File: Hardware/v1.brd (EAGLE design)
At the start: 77.5 x 32.6 mm, 54 parts, among them CN1 629105150521, CN2 TSW-120-08-L-S-RA, CN3 1734354-1, CN4 1-1734530-1, IC1 ADUM3160BRWZ, IC2 TUSB2046BIRHBT, IC3 IC_MAX3313, IC4 FT2232D, IC6 PCM2903C

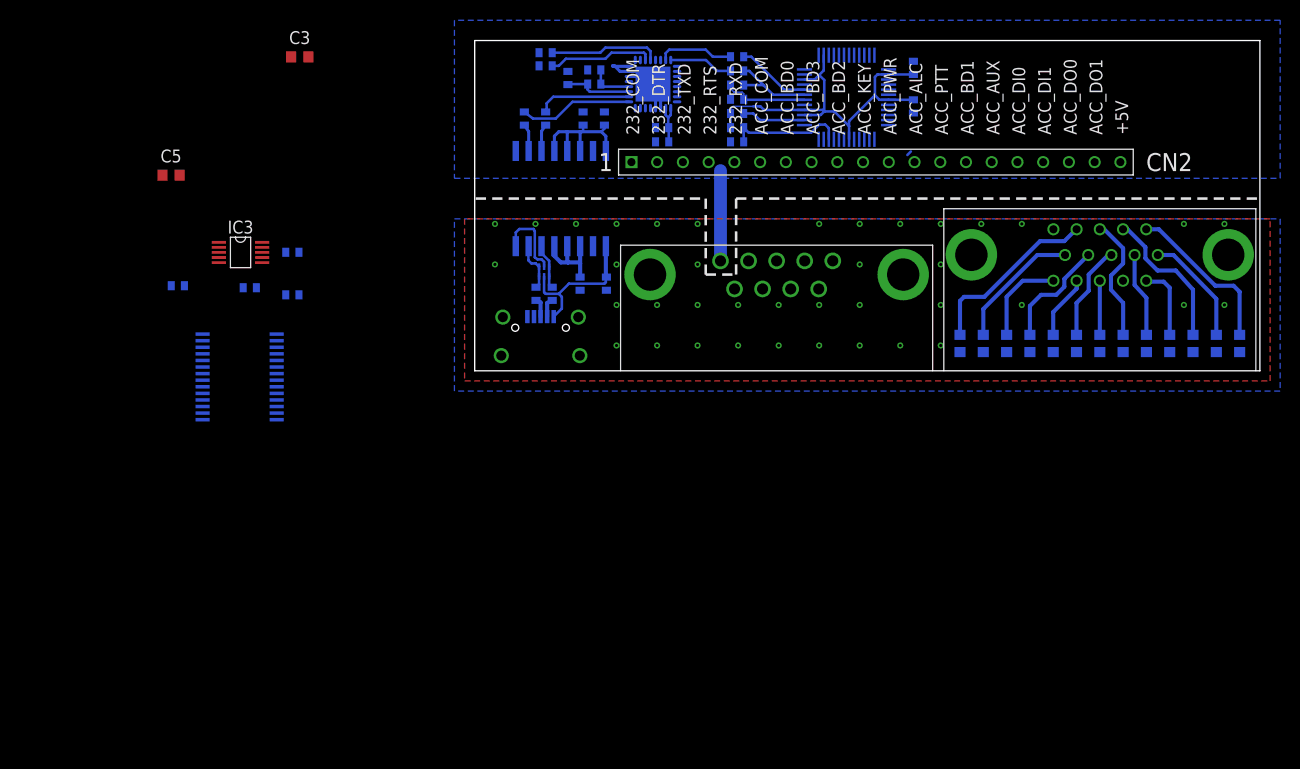
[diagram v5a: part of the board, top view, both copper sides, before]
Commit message: mirrored digital section of board to allow for easier routing to io
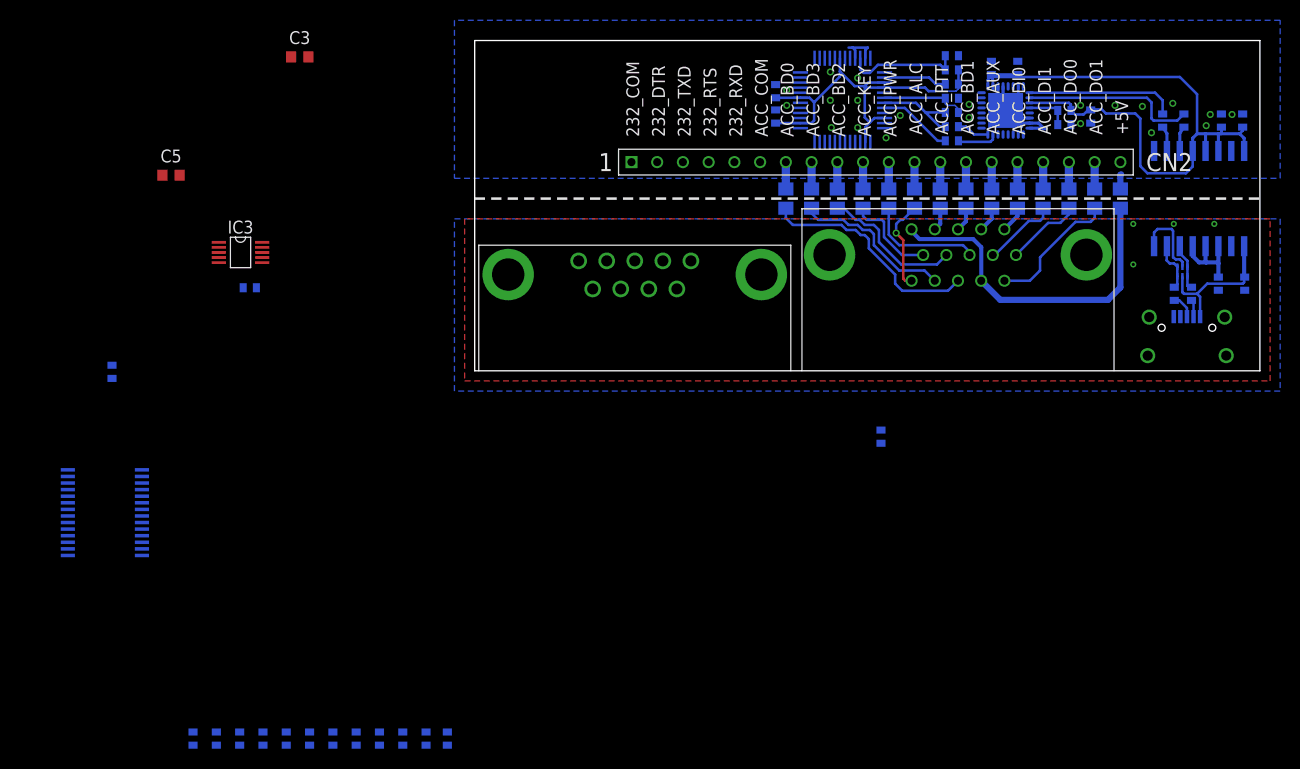
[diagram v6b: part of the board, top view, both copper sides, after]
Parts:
- removed R12, R13, R8, R9: 24, rcl:R0402
- added L1: 100uH, m0wut:R0805
- added R17, R18, R19, R20, R21, R22, R23, R24, R25, R26, R27, R28: 220, rcl:R0805
- added R29: 137k, rcl:R0805
- C12, C13, C14, C15, C16, C17, C18, C19, C20, C21, C22, C23, C24: device rcl:C0603 -> rcl:C0402
- moved C12 87.4 mm to (-2.70, -36.3)
- moved C13 87.2 mm to (-7.10, -36.3)
- moved C14 87.2 mm to (-14.0, -36.3)
- moved C16 87.2 mm to (-4.80, -36.3)
- moved C17 87.2 mm to (-11.7, -36.3)
- moved C18 87.2 mm to (-18.6, -36.3)
- moved C19 87.2 mm to (-23.2, -36.3)
- moved C20 87.2 mm to (-27.8, -36.3)
- moved C21 87.2 mm to (-9.40, -36.3)
- moved C22 87.2 mm to (-16.3, -36.3)
- moved C23 87.2 mm to (-20.9, -36.3)
- moved C24 87.2 mm to (-25.5, -36.3)
- moved CN1 63.8 mm to (70.3, 0.00)
- moved R2 63.1 mm to (70.8, 7.60)
- moved R4 63.0 mm to (67.9, 24.7)
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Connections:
- net N$4 renamed USB4_P
- net N$5 renamed USB4_N
- removed net DM1: R8.1
- removed net DM3: R13.2
- removed net DP1: R9.1
- removed net DP3: R12.2
- removed net N$18: C23.1, CN4.14
- removed net N$19: CN4.12
- removed net N$20: CN4.5
- removed net N$21: C24.1, CN4.15
- removed net N$22: C22.1, CN4.13
- removed net N$23: C21.1, CN4.11
- removed net N$24: C20.1, CN4.10
- removed net N$25: C19.1, CN4.9
- removed net N$26: C18.1, CN4.8
- removed net N$27: C17.1, CN4.7
- removed net N$28: C16.1, CN4.6
- removed net N$29: C15.1, CN4.4
- removed net N$30: C14.1, CN4.3
- removed net N$31: C13.1, CN4.2
- removed net N$32: C12.1, CN4.1
- new net 232_COM: CN2.P$1
- new net 232_DTR: CN2.P$2
- new net 232_RTS: CN2.P$4
- new net 232_RXD: CN2.P$5
- new net 232_TXD: CN2.P$3
- new net 5V_IN: CN2.P$20
- new net ACC_ALC: CN2.P$12, R29.1
- new net ACC_AUX: CN2.P$15, R18.1
- new net ACC_BND0: CN2.P$7, R27.1
- new net ACC_BND1: CN2.P$14, R19.1
- new net ACC_BND2: CN2.P$9, R24.1
- new net ACC_BND3: CN2.P$8, R28.1
- new net ACC_COM: CN2.P$6
- new net ACC_COMMON: CN4.12, CN4.5, L1.2
- new net ACC_DI0: CN2.P$16, R17.1
- new net ACC_DI1: CN2.P$17, R22.1
- new net ACC_DO0: CN2.P$18, R21.1
- new net ACC_DO1: CN2.P$19, R26.1
- new net ACC_KEY: CN2.P$10, R25.1
- new net ACC_PTT: CN2.P$13, R20.1
- new net ACC_PWR: CN2.P$11, R23.1
- new net ALC_X: C24.1, CN4.15, R29.2
- new net AUX_X: C13.1, CN4.2, R18.2
- new net BND0_X: C22.1, CN4.13, R27.2
- new net BND1_X: C14.1, CN4.3, R19.2
- new net BND2_X: C19.1, CN4.9, R24.2
- new net BND3_X: C23.1, CN4.14, R28.2
- new net DIG0_X: C12.1, CN4.1, R17.2
- new net DIG1_X: C17.1, CN4.7, R22.2
- new net DIGO1_X: C21.1, CN4.11, R26.2
- new net DIGO_X: C16.1, CN4.6, R21.2
- new net KEY_X: C20.1, CN4.10, R25.2
- new net PTT_X: C15.1, CN4.4, R20.2
- new net PWR_X: C18.1, CN4.8, R23.2
- net GND: now also L1.1
- net N$12: no longer R8.2
- net N$13: no longer R9.2
- net N$16: no longer R12.1
- net N$17: no longer R13.1
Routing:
- net +3V3: track 24.8 -> 68.5 mm
- net ACC_COMMON: track 0.00 -> 33.9 mm
- net BND0_X: track 0.00 -> 22.4 mm
- net N$29: track 17.8 -> 0.00 mm
- net BND3_X: track 0.00 -> 16.1 mm
- net N$32: track 16.0 -> 0.00 mm
- net N$31: track 14.5 -> 0.00 mm
- net BND2_X: track 0.00 -> 14.4 mm
- net DIGO1_X: track 0.00 -> 13.2 mm
- net N$24: track 12.8 -> 0.00 mm
- net N$30: track 12.6 -> 0.00 mm
- net PWR_X: track 0.00 -> 11.6 mm
- net N$28: track 11.1 -> 0.00 mm
- net N$25: track 11.1 -> 0.00 mm
- net N$13: track 10.9 -> 0.00 mm
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
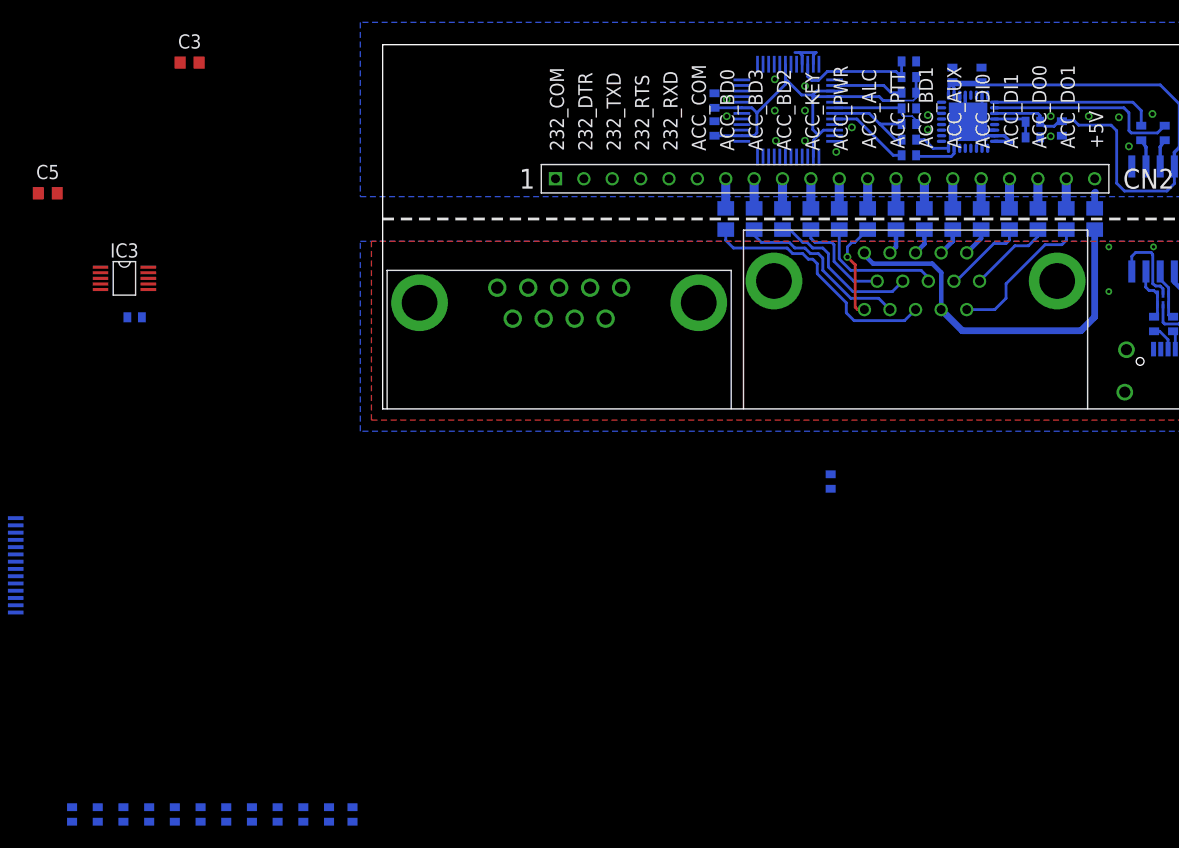
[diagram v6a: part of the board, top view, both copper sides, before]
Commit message: finally got the decoupling caps for the db15 to fit
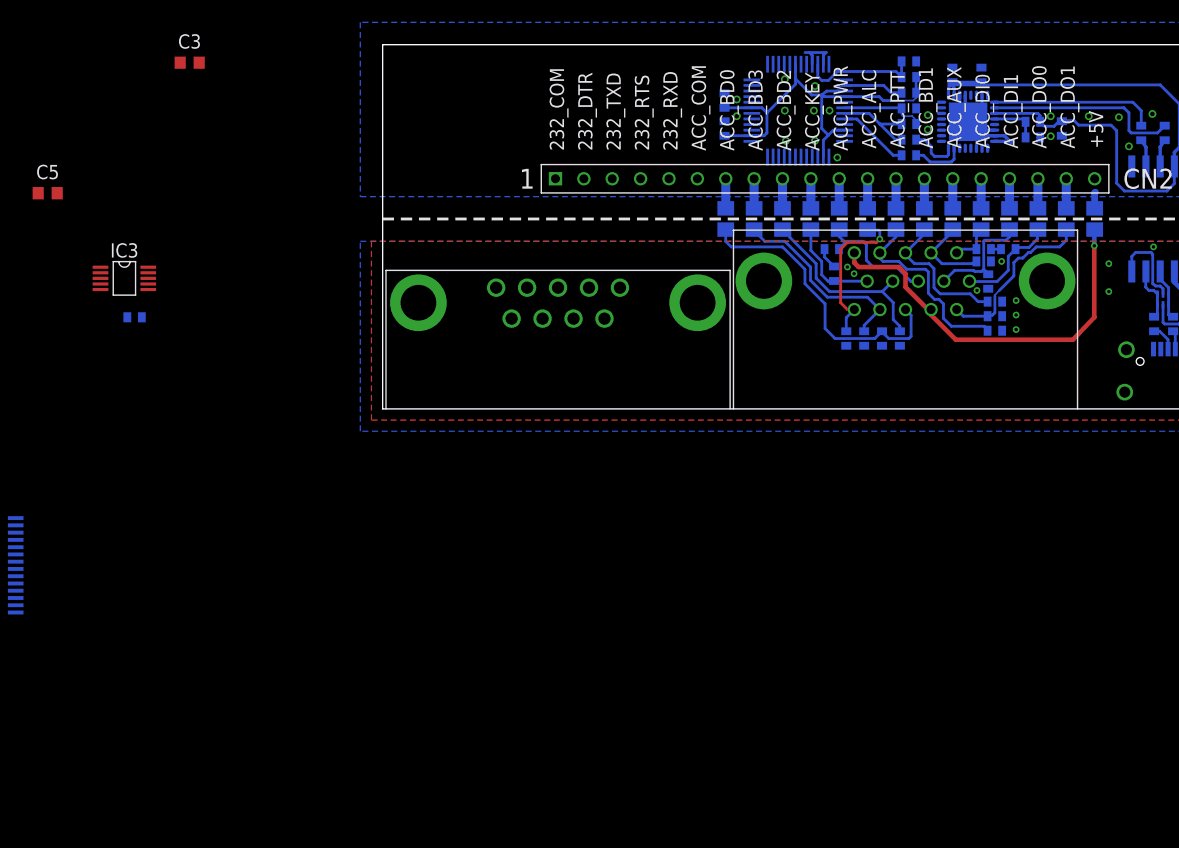
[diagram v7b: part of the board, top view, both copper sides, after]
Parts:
- moved C20 83.6 mm to (40.4, 12.1), turned to 90 degrees
- moved C14 82.7 mm to (54.8, 9.60), turned to 180 degrees
- moved C19 81.5 mm to (46.3, 6.30)
- moved C17 81.4 mm to (54.2, 11.4)
- moved C24 79.4 mm to (41.5, 6.30)
- moved C16 79.1 mm to (56.0, 14.3), turned to 0 degrees
- moved C13 78.5 mm to (53.8, 13.2), turned to 180 degrees
- moved C21 78.2 mm to (54.8, 8.30), turned to 180 degrees
- moved C18 77.6 mm to (40.2, 14.3), turned to 0 degrees
- moved C23 76.9 mm to (43.1, 6.30)
- moved C12 75.8 mm to (53.8, 14.3), turned to 180 degrees
- moved C22 74.4 mm to (44.7, 6.30)
- moved C15 20.0 mm to (54.8, 7.00), turned to 180 degrees
- moved CN4 0.90 mm to (46.8, 0.00)
- moved IC4 0.90 mm to (37.2, 26.7)
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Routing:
- net PTT_X: track 2.30 -> 17.4 mm
- net BND1_X: track 2.41 -> 13.0 mm
- net ALC_X: track 9.05 -> 14.2 mm
- net AUX_X: track 2.51 -> 7.43 mm
- net BND0_X: track 22.4 -> 26.5 mm
- net BND2_X: track 14.4 -> 18.4 mm
- net AGND: track 7.65 -> 10.7 mm, vias 4 -> 11
- net DIG1_X: track 7.44 -> 10.4 mm
- net DIGO_X: track 7.49 -> 9.93 mm
- net DIGO1_X: track 13.2 -> 15.5 mm
- net BND3_X: track 16.1 -> 17.5 mm
- net DIG0_X: track 2.61 -> 3.98 mm
- net N$15: track 3.22 -> 4.51 mm
- net ACC_COMMON: track 33.9 -> 34.9 mm, vias 0 -> 1
- net N$33: track 11.6 -> 10.7 mm
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
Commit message: reorganised decoupling caps to be slightly less crazy
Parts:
- moved C16 3.79 mm to (54.8, 10.7), turned to 180 degrees
- moved C17 2.18 mm to (54.8, 9.30), turned to 180 degrees
- moved C15 1.90 mm to (54.8, 5.10)
- moved C21 1.80 mm to (54.8, 6.50)
- moved C14 1.70 mm to (54.8, 7.90)
- moved C20 1.64 mm to (39.1, 13.1), turned to 270 degrees
- moved C18 1.24 mm to (40.5, 13.1), turned to 270 degrees
- moved C24 0.40 mm to (41.9, 6.30)
- moved C13 0.20 mm to (53.8, 13.0)
- moved C19 0.20 mm to (46.1, 6.30)
- moved C23 0.20 mm to (43.3, 6.30)
- moved C12 0.10 mm to (53.8, 14.4)
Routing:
- net DIG1_X: track 10.4 -> 14.5 mm
- net AGND: track 10.7 -> 7.80 mm, vias 11 -> 19
- net DIGO1_X: track 15.5 -> 18.0 mm
- net BND3_X: track 17.5 -> 18.6 mm
- net BND2_X: track 18.4 -> 19.3 mm
- net KEY_X: track 8.86 -> 7.99 mm
- net PTT_X: track 17.4 -> 18.1 mm
- net BND1_X: track 13.0 -> 13.7 mm
- net PWR_X: track 11.1 -> 11.8 mm
- net GND: vias 21 -> 24
